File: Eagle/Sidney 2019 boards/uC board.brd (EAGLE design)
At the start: 100 x 100 mm, 56 parts, among them J1 39-28-1043

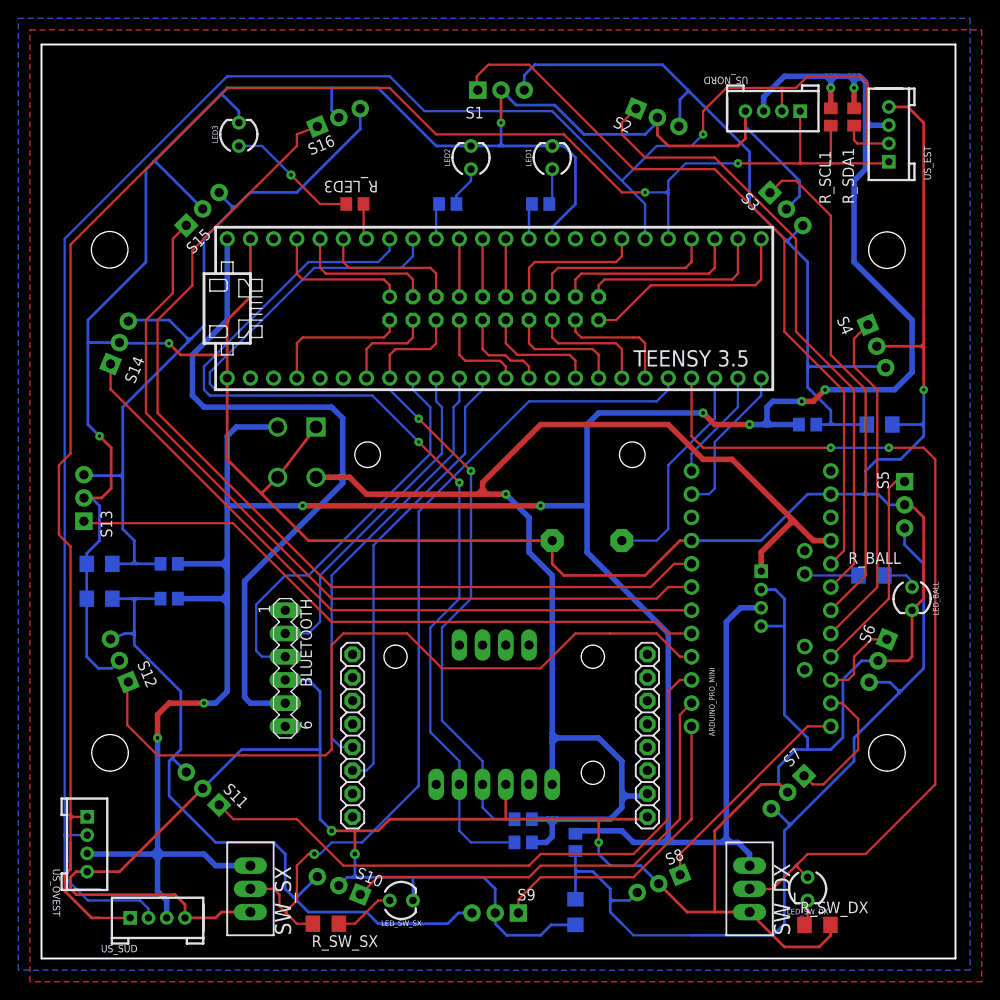
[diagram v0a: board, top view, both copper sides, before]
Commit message: Created line sensors layout for gerber generation. Added logos to uC and motor PCBs. Generater and uploaded on PCBWAY every gerber
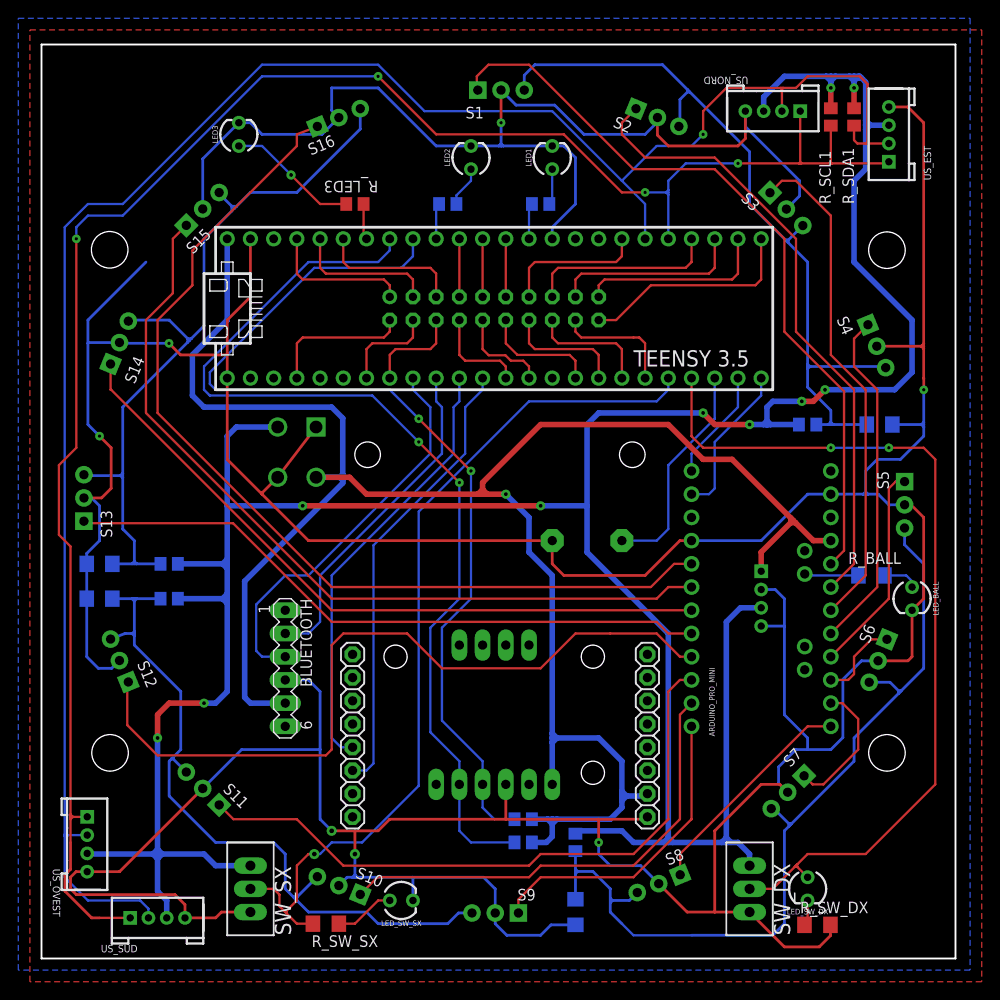
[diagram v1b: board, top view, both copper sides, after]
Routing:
- net GND: track 675.0 -> 651.7 mm
- net SCL1: track 202.8 -> 204.6 mm, vias 2 -> 4
- net SDA1: track 213.7 -> 215.5 mm

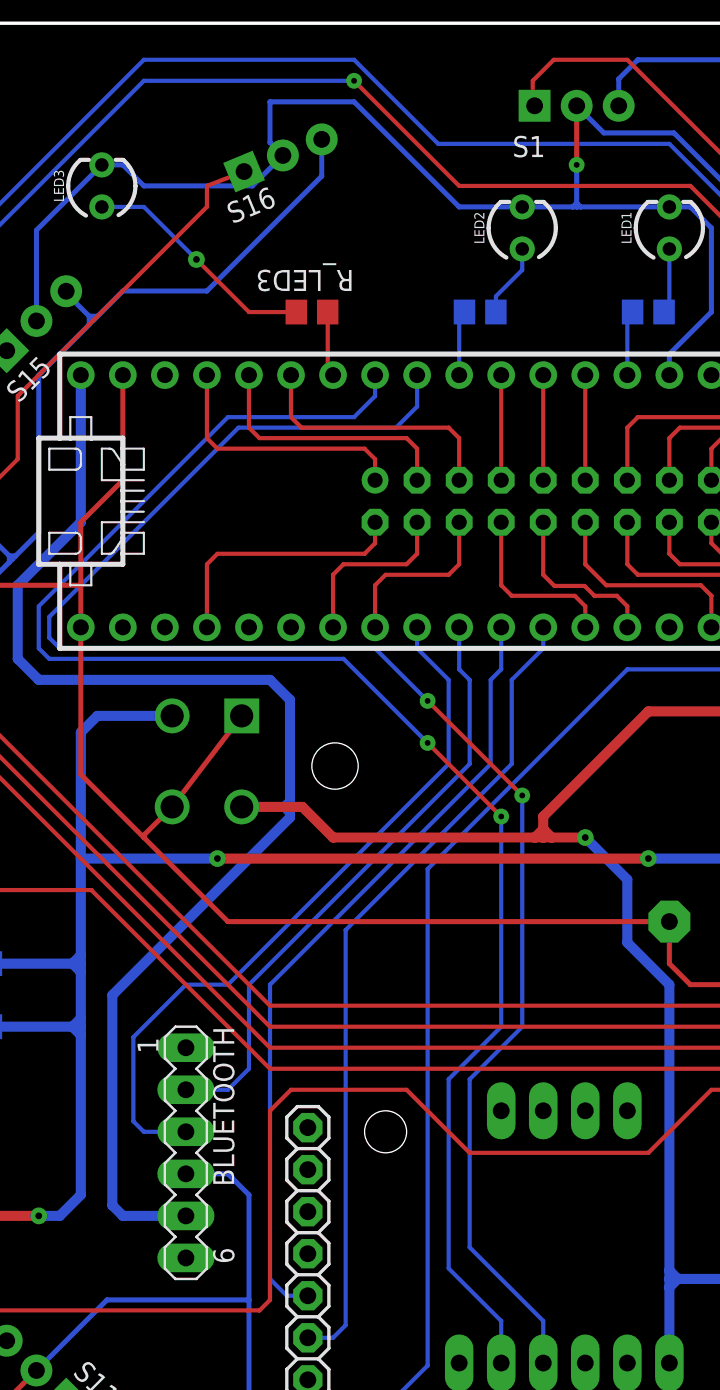
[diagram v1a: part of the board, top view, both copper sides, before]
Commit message: Added issues list, fixed uC board short to ground
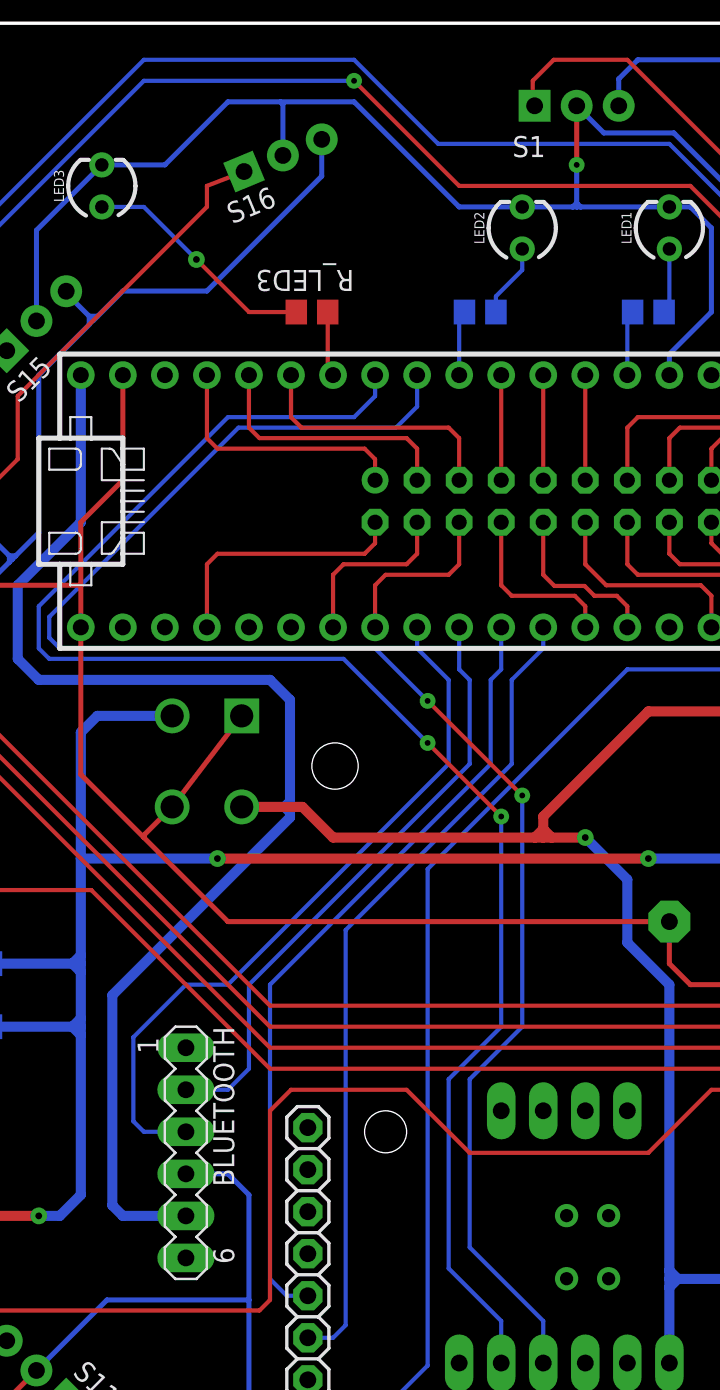
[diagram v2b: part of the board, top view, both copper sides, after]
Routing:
- net GND: track 651.7 -> 650.9 mm
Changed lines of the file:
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@@
 <drawing>
 <settings>
-<setting alwaysvectorfont="yes"/>
+<setting alwaysvectorfont="no"/>
 <setting verticaltext="up"/>
 </settings>
-<grid distance="0.05" unitdist="mm" unit="mm" style="lines" multiple="1" display="yes" altdistance="25" altunitdist="mil" altunit="mil"/>
+<grid distance="50" unitdist="mil" unit="mil" style="lines" multiple="1" display="yes" altdistance="25" altunitdist="mil" altunit="mil"/>
 <layers>
 <layer number="1" name="Top" color="4" fill="1" visible="yes" active="yes"/>
@@
 <wire x1="13.9508" y1="67.31" x2="15.2208" y2="66.04" width="0.3048" layer="1"/>
 <wire x1="15.2208" y1="66.04" x2="20.32" y2="66.04" width="0.3048" layer="1"/>
-<wire x1="31.75" y1="95.25" x2="36.83" y2="95.25" width="0.3048" layer="16"/>
-<wire x1="31.75" y1="92.79" x2="32.53" y2="92.01" width="0.3048" layer="16"/>
-<wire x1="31.75" y1="95.25" x2="31.75" y2="92.79" width="0.3048" layer="16"/>
 <wire x1="50.28" y1="95.01" x2="50.28" y2="91.44" width="0.3048" layer="1"/>
 <via x="50.28" y="91.44" extent="1-16" drill="0.35"/>
@@
 <wire x1="4.64" y1="50.39" x2="6.575" y2="50.39" width="0.3048" layer="1"/>
 <wire x1="6.575" y1="50.39" x2="7.62" y2="51.435" width="0.3048" layer="1"/>
-<wire x1="32.53" y1="92.01" x2="30.69" y2="90.17" width="0.3048" layer="16"/>
-<wire x1="24.13" y1="90.17" x2="30.69" y2="90.17" width="0.3048" layer="16"/>
 <wire x1="43.18" y1="88.9" x2="46.99" y2="88.9" width="0.3048" layer="16"/>
 <wire x1="36.83" y1="95.25" x2="43.18" y2="88.9" width="0.3048" layer="16"/>
@@
 <wire x1="85.09" y1="1.27" x2="86.3215" y2="2.5015" width="0.3048" layer="1"/>
 <wire x1="86.3215" y1="2.5015" x2="86.3215" y2="3.683" width="0.3048" layer="1"/>
-<wire x1="21.59" y1="91.44" x2="22.86" y2="91.44" width="0.3048" layer="16"/>
-<wire x1="22.86" y1="91.44" x2="24.13" y2="90.17" width="0.3048" layer="16"/>
 <wire x1="21.59" y1="91.44" x2="17.64" y2="87.49" width="0.3048" layer="16"/>
 <wire x1="17.64" y1="87.49" x2="17.64" y2="82.01" width="0.3048" layer="16"/>
+<wire x1="25.4" y1="91.44" x2="29.21" y2="95.25" width="0.3048" layer="16"/>
+<wire x1="21.59" y1="91.44" x2="25.4" y2="91.44" width="0.3048" layer="16"/>
+<wire x1="29.21" y1="95.25" x2="32.385" y2="95.25" width="0.3048" layer="16"/>
+<wire x1="32.385" y1="95.25" x2="36.83" y2="95.25" width="0.3048" layer="16"/>
+<wire x1="32.53" y1="92.01" x2="32.53" y2="95.105" width="0.3048" layer="16"/>
+<wire x1="32.53" y1="95.105" x2="32.385" y2="95.25" width="0.3048" layer="16"/>
 </signal>
 <signal name="SP3">
@@
 <wire x1="83.82" y1="4.0255" x2="83.4775" y2="3.683" width="0.254" layer="1"/>
 </signal>
+<signal name="GND1" class="1">
+<via x="49.67" y="24.145" extent="1-16" drill="0.8"/>
+<via x="52.21" y="24.145" extent="1-16" drill="0.8"/>
+<via x="49.67" y="27.955" extent="1-16" drill="0.8"/>
+<via x="52.21" y="27.955" extent="1-16" drill="0.8"/>
+<wire x1="49.67" y1="27.955" x2="52.21" y2="27.955" width="0" layer="19" extent="1-1"/>
+<wire x1="52.21" y1="24.145" x2="52.21" y2="27.955" width="0" layer="19" extent="1-1"/>
+<wire x1="49.67" y1="24.145" x2="52.21" y2="24.145" width="0" layer="19" extent="1-1"/>
+</signal>
 </signals>
